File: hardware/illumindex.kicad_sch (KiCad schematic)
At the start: 4 parts, among them SW1 SW_MEC_5G, SW2 SW_SPDT

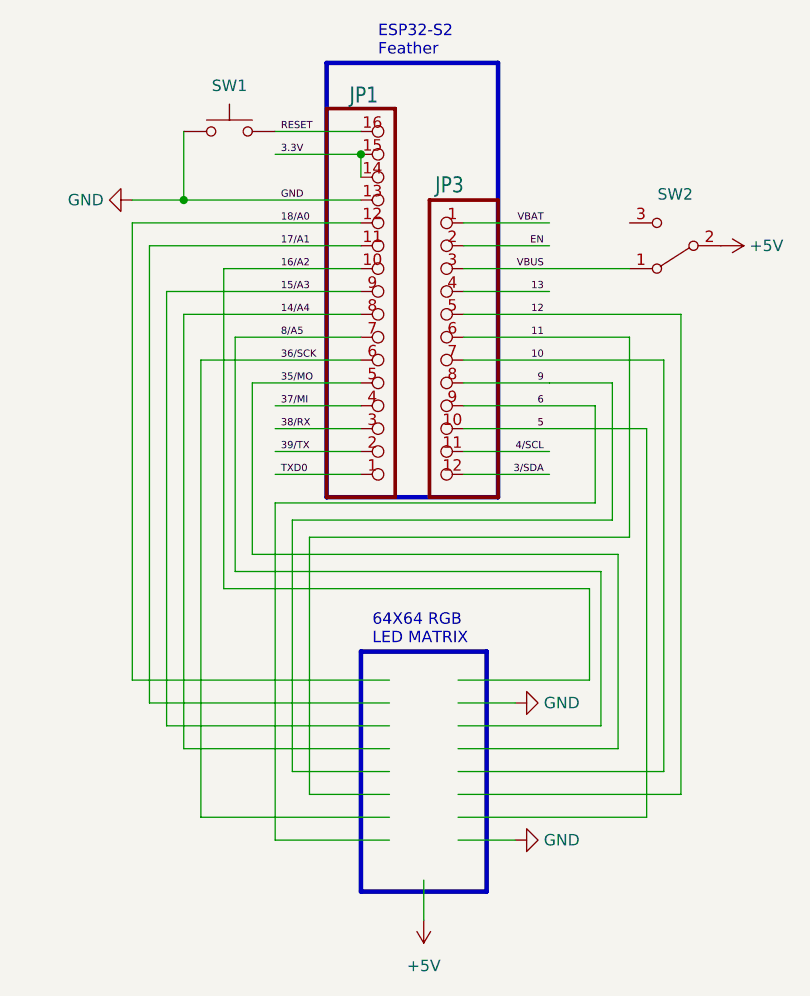
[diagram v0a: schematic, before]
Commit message: Update pins for hardware change
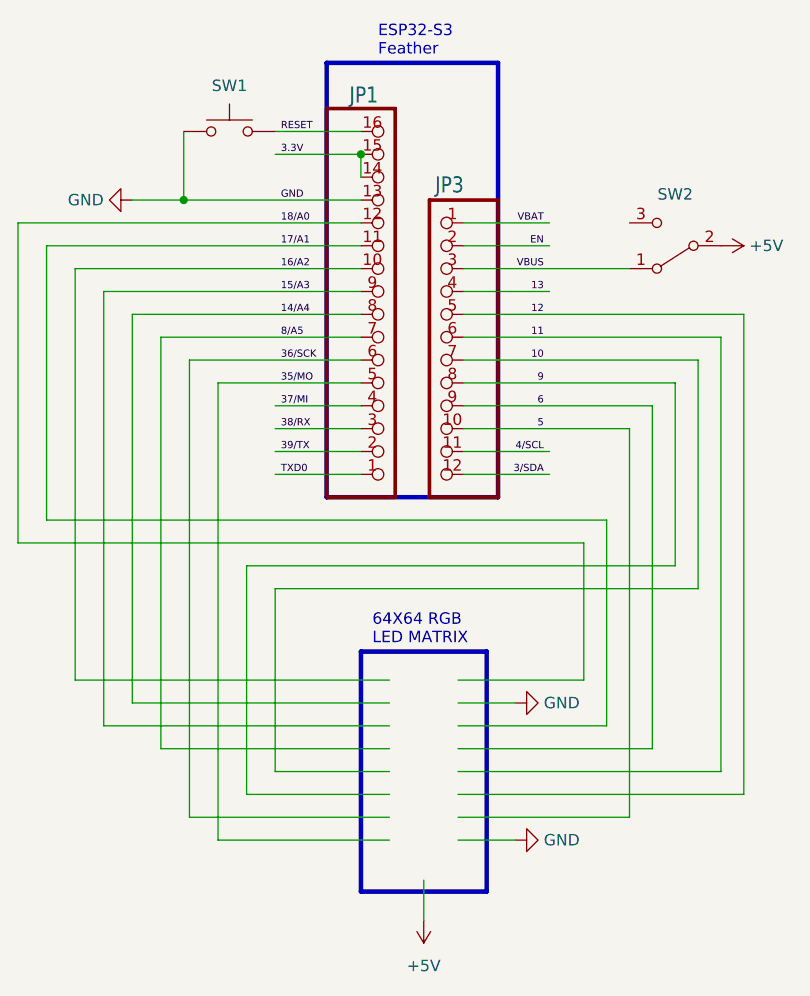
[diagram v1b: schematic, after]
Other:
- note added: "ESP32-S3 Feather"
- note removed: "ESP32-S2 Feather"
